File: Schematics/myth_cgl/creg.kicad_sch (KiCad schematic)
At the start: 11 parts, among them U10 74HC00, U11 74AHC273, U12 4078, U13 74LS573, U14 74AHC244, U21 74HC04, U3 74LS32, U5 74LS08, U7 74HC02, U8 74HC74, U9 74AHC273

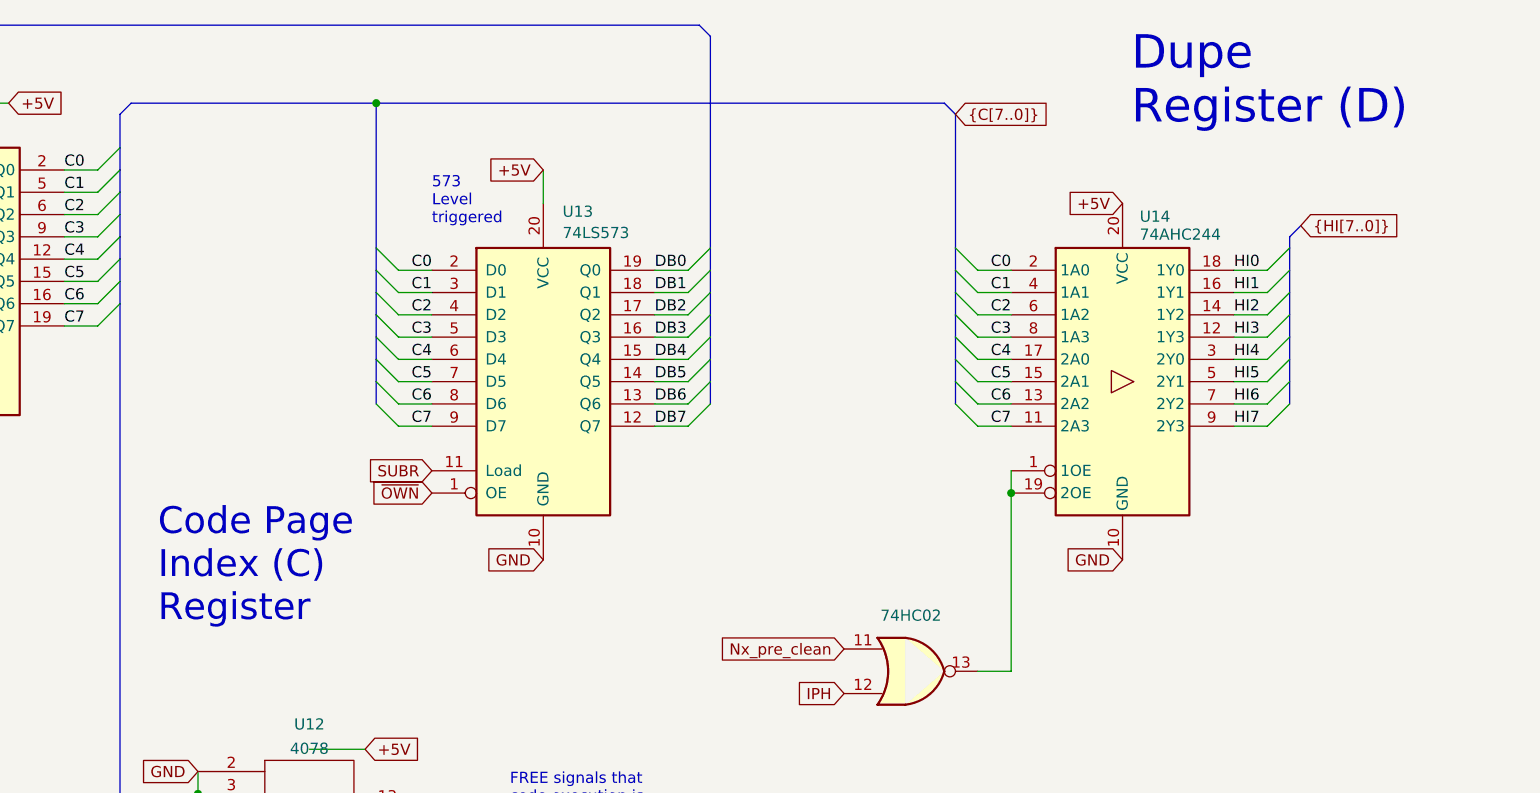
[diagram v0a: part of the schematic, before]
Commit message: Change semantics of xB
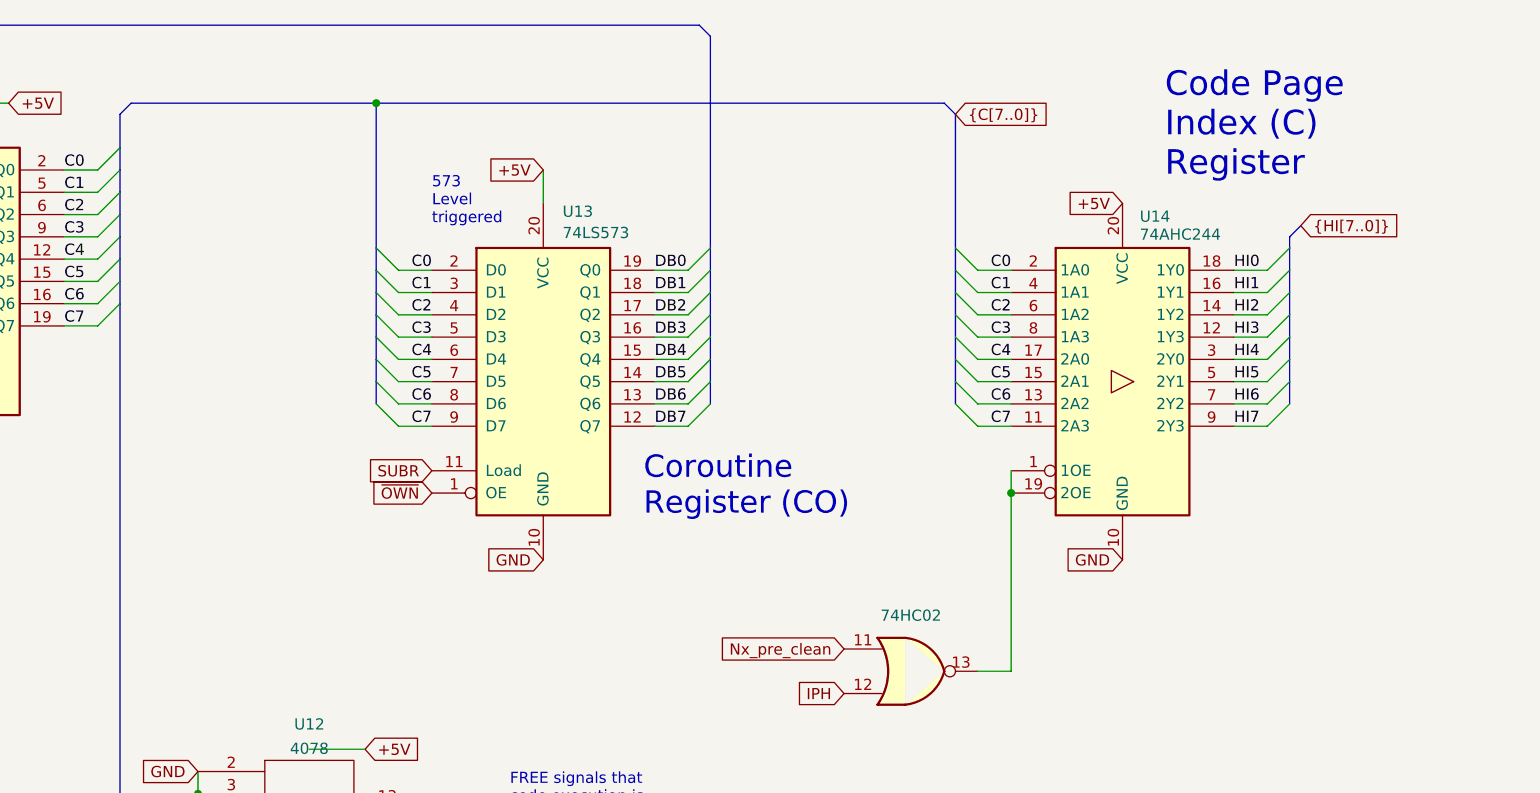
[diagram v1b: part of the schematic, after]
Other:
- note added: "Coroutine Register (CO)"
- note removed: "Dupe Register (D)"
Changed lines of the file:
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@@
 	(text "Code Page\nIndex (C)\nRegister"
 		(exclude_from_sim no)
-		(at 131.318 92.456 0)
+		(at 246.126 41.656 0)
 		(effects
 			(font
-				(size 3.048 3.048)
+				(size 2.794 2.794)
 			)
 			(justify left bottom)
@@
 		)
 	)
-	(text "Dupe\nRegister (D)"
+	(text "Coroutine\nRegister (CO)"
 		(exclude_from_sim no)
-		(at 242.316 35.814 0)
+		(at 186.69 80.264 0)
 		(effects
 			(font
-				(size 3.81 3.81)
+				(size 2.54 2.54)
 			)
 			(justify left bottom)
